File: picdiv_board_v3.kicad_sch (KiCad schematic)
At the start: 64 parts, among them J1 DC-Input, J10 PPS_B, J101 MountingHole_M2.5, J104 MountingHole_M2.5, J105 Conn_01x06, J106 PPS_A, J107 PPS_A, J14 TEST_1PPS, J4 SYNC, J6 PPS_B, J8 SYNC, SW101 SW_DIP_x03, U1 LT1963AxST-3.3, U103 LT1963AEQ, U104 LTC6993xS6-1, U105 IDT5PB1108, U2 LT1963AxST-3.3, U3 PIC12F675, U6 IDT5PB1108

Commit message: Remove redundant items.
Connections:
- net +6V renamed +5V
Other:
- note added: "5VDC for OXCO"
- note removed: "6VDC for sine-to-square"
- title: PICDIV - PPS-board - v3 -> PICDIV - PPS-board - v4 AF
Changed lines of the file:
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@@
 	(paper "A4")
 	(title_block
-		(title "PICDIV - PPS-board - v3")
-		(rev "2019-01")
+		(title "PICDIV - PPS-board - v4 AF")
+		(date "2024-11-19")
+		(rev "2024-11")
 		(company "anders.e.e.wallin \"at\" gmail.com")
 		(comment 1 "2018-08-01 first proto-boards order")
@@
 	)
 	(junction
+		(at 162.56 163.83)
+		(diameter 0)
+		(color 0 0 0 0)
+	)
+	(junction
 		(at 232.41 50.8)
 		(diameter 0)
@@
 	)
 	(junction
-		(at 161.29 163.83)
-		(diameter 0)
-		(color 0 0 0 0)
-	)
-	(junction
 		(at 140.97 140.97)
 		(diameter 0)
@@
 	(wire
 		(pts
-			(xy 161.29 163.83) (xy 161.29 161.29)
+			(xy 162.56 163.83) (xy 162.56 162.56)
 		)
 		(stroke
@@
 	(wire
 		(pts
+			(xy 162.56 163.83) (xy 163.83 163.83)
+		)
+		(stroke
+			(width 0)
+			(type default)
+		)
+	)
+	(wire
+		(pts
 			(xy 68.58 137.16) (xy 69.85 137.16)
 		)
@@
 	(wire
 		(pts
-			(xy 161.29 163.83) (xy 163.83 163.83)
-		)
-		(stroke
-			(width 0)
-			(type default)
-		)
-	)
-	(wire
-		(pts
 			(xy 115.57 53.34) (xy 121.92 53.34)
 		)
@@
 	(wire
 		(pts
-			(xy 151.13 163.83) (xy 161.29 163.83)
+			(xy 151.13 163.83) (xy 162.56 163.83)
 		)
 		(stroke
@@
 		)
 	)
-	(text "6VDC for sine-to-square"
+	(text "5VDC for OXCO"
 		(exclude_from_sim no)
 		(at 134.62 162.56 0)
@@
 	)
 	(symbol
-		(lib_id "power:+6V")
-		(at 161.29 161.29 0)
-		(unit 1)
-		(exclude_from_sim no)
-		(in_bom yes)
-		(on_board yes)
-		(dnp no)
-		(property "Reference" "#PWR017"
-			(at 161.29 165.1 0)
-			(effects
-				(font
-					(size 1.27 1.27)
-				)
-				(hide yes)
-			)
-		)
-		(property "Value" "+6V"
-			(at 161.29 157.734 0)
-			(effects
-				(font
-					(size 1.27 1.27)
-				)
-			)
-		)
-		(property "Footprint" ""
-			(at 161.29 161.29 0)
-			(effects
-				(font
-					(size 1.27 1.27)
-				)
-				(hide yes)
-			)
-		)
-		(property "Datasheet" ""
-			(at 161.29 161.29 0)
-			(effects
-				(font
-					(size 1.27 1.27)
-				)
-				(hide yes)
-			)
-		)
-		(property "Description" ""
-			(at 161.29 161.29 0)
-			(effects
-				(font
-					(size 1.27 1.27)
-				)
-				(hide yes)
-			)
-		)
-		(pin "1"
-		)
-		(instances
-			(project "picdiv_board_v3"
-				(path "/eba36321-b5f3-4bd6-a805-57b9b2ee447e"
-					(reference "#PWR017")
-					(unit 1)
-				)
-			)
-		)
-	)
-	(symbol
 		(lib_id "Device:D")
 		(at 31.75 163.83 180)
@@
 					(unit 1)
 				)
+			)
+		)
+	)
+	(symbol
+		(lib_id "power:+5V")
+		(at 162.56 162.56 0)
+		(unit 1)
+		(exclude_from_sim no)
+		(in_bom yes)
+		(on_board yes)
+		(dnp no)
+		(fields_autoplaced yes)
+		(property "Reference" "#PWR01"
+			(at 162.56 166.37 0)
+			(effects
+				(font
+					(size 1.27 1.27)
+				)
+				(hide yes)
+			)
+		)
+		(property "Value" "+5V"
+			(at 162.56 157.48 0)
+			(effects
+				(font
+					(size 1.27 1.27)
+				)
+			)
+		)
+		(property "Footprint" ""
+			(at 162.56 162.56 0)
+			(effects
+				(font
+					(size 1.27 1.27)
+				)
+				(hide yes)
+			)
+		)
+		(property "Datasheet" ""
+			(at 162.56 162.56 0)
+			(effects
+				(font
+					(size 1.27 1.27)
+				)
+				(hide yes)
+			)
+		)
+		(property "Description" "Power symbol creates a global label with name \"+5V\""
+			(at 162.56 162.56 0)
+			(effects
+				(font
+					(size 1.27 1.27)
+				)
+				(hide yes)
+			)
+		)
+		(pin "1"
+		)
+		(instances
+			(project ""
+				(path "/eba36321-b5f3-4bd6-a805-57b9b2ee447e"
+					(reference "#PWR01")
+					(unit 1)
+				)

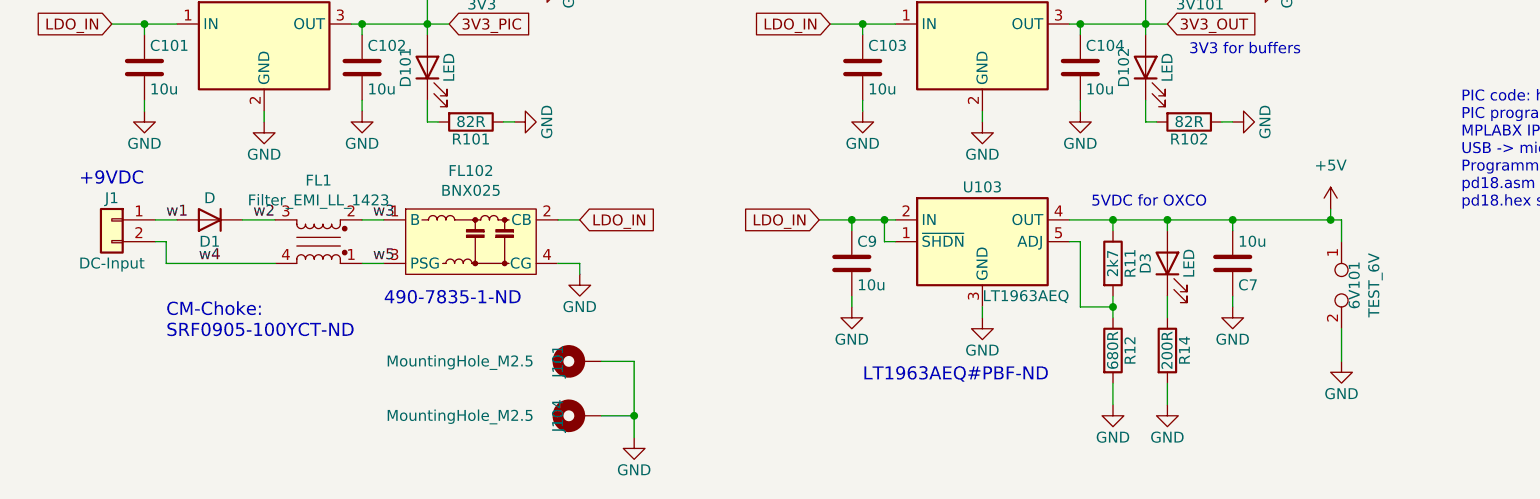
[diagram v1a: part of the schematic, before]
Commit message: 5.0V LDO for OXCO.
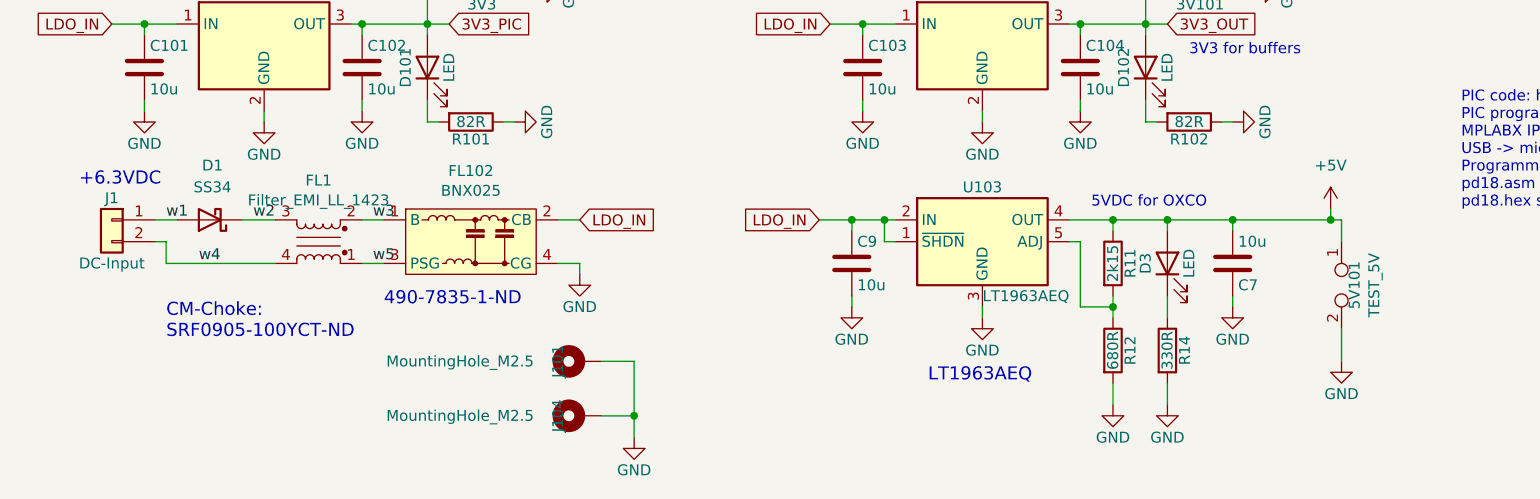
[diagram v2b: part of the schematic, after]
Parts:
- removed D1: D, awallinKiCadFootprints:DIODE_DO-214BA, symbol Device:D
- added D1: SS34, Diode_SMD:D_SMA, symbol Diode:SS34
- 5V101: renamed from 6V101; value TEST_6V -> TEST_5V
- R11: value 2k7 -> 2k15
- R14: value 200R -> 330R
- U103: LCSC (none) -> C459702
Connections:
- net w1: now also D1.2 (A)
- net w2: now also D1.1 (K)
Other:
- note added: "+6.3VDC"
- note added: "LT1963AEQ"
- note removed: "+9VDC"
- note removed: "LT1963AEQ#PBF-ND"
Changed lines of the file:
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@@
 		)
 	)
-	(text "LT1963AEQ#PBF-ND"
+	(text "LT1963AEQ"
 		(exclude_from_sim no)
-		(at 107.95 182.88 0)
+		(at 115.57 182.88 0)
 		(effects
 			(font
@@
 		)
 	)
-	(text "+9VDC"
+	(text "+6.3VDC"
 		(exclude_from_sim no)
 		(at 16.51 160.02 0)
@@
 			)
 		)
-		(property "Value" "2k7"
+		(property "Value" "2k15"
 			(at 137.16 168.91 90)
 			(effects
@@
 			)
 		)
-		(property "Value" "200R"
+		(property "Value" "330R"
 			(at 143.51 179.07 90)
 			(effects
@@
 	)
 	(symbol
-		(lib_id "Device:D")
-		(at 31.75 163.83 180)
-		(unit 1)
-		(exclude_from_sim no)
-		(in_bom yes)
-		(on_board yes)
-		(dnp no)
-		(property "Reference" "D1"
-			(at 31.75 166.37 0)
-			(effects
-				(font
-					(size 1.27 1.27)
-				)
-			)
-		)
-		(property "Value" "D"
-			(at 31.75 161.29 0)
-			(effects
-				(font
-					(size 1.27 1.27)
-				)
-			)
-		)
-		(property "Footprint" "awallinKiCadFootprints:DIODE_DO-214BA"
-			(at 31.75 163.83 0)
-			(effects
-				(font
-					(size 1.27 1.27)
-				)
-				(hide yes)
-			)
-		)
-		(property "Datasheet" ""
-			(at 31.75 163.83 0)
-			(effects
-				(font
-					(size 1.27 1.27)
-				)
-				(hide yes)
-			)
-		)
-		(property "Description" ""
-			(at 31.75 163.83 0)
-			(effects
-				(font
-					(size 1.27 1.27)
-				)
-				(hide yes)
-			)
-		)
-		(pin "1"
-		)
-		(pin "2"
-		)
-		(instances
-			(project "picdiv_board_v3"
-				(path "/eba36321-b5f3-4bd6-a805-57b9b2ee447e"
-					(reference "D1")
-					(unit 1)
-				)
-			)
-		)
-	)
-	(symbol
 		(lib_id "Device:R")
 		(at 134.62 41.91 0)
@@
 		(on_board yes)
 		(dnp no)
-		(property "Reference" "6V101"
+		(property "Reference" "5V101"
 			(at 165.354 171.45 0)
 			(effects
@@
 			)
 		)
-		(property "Value" "TEST_6V"
+		(property "Value" "TEST_5V"
 			(at 167.64 171.45 0)
 			(effects
@@
 			(project "picdiv_board_v3"
 				(path "/eba36321-b5f3-4bd6-a805-57b9b2ee447e"
-					(reference "6V101")
+					(reference "5V101")
 					(unit 1)
 				)
@@
 			)
 		)
+		(property "LCSC" "C459702 "
+			(at 121.92 166.37 0)
+			(effects
+				(font
+					(size 1.27 1.27)
+				)
+				(hide yes)
+			)
+		)
 		(pin "1"
 		)
@@
 					(unit 1)
 				)
+			)
+		)
+	)
+	(symbol
+		(lib_id "Diode:SS34")
+		(at 31.75 163.83 180)
+		(unit 1)
+		(exclude_from_sim no)
+		(in_bom yes)
+		(on_board yes)
+		(dnp no)
+		(fields_autoplaced yes)
+		(property "Reference" "D1"
+			(at 32.0675 157.48 0)
+			(effects
+				(font
+					(size 1.27 1.27)
+				)
+			)
+		)
+		(property "Value" "SS34"
+			(at 32.0675 160.02 0)
+			(effects
+				(font
+					(size 1.27 1.27)
+				)
+			)
+		)
+		(property "Footprint" "Diode_SMD:D_SMA"
+			(at 31.75 159.385 0)
+			(effects
+				(font
+					(size 1.27 1.27)
+				)
+				(hide yes)
+			)
+		)
+		(property "Datasheet" "https://www.vishay.com/docs/88751/ss32.pdf"
+			(at 31.75 163.83 0)
+			(effects
+				(font
+					(size 1.27 1.27)
+				)
+				(hide yes)
+			)
+		)
+		(property "Description" "40V 3A Schottky Diode, SMA"
+			(at 31.75 163.83 0)
+			(effects
+				(font
+					(size 1.27 1.27)
+				)
+				(hide yes)
+			)
+		)
+		(property "LCSC" "C8678"
+			(at 31.75 163.83 0)
+			(effects
+				(font
+					(size 1.27 1.27)
+				)
+				(hide yes)
+			)
+		)
+		(pin "2"
+		)
+		(pin "1"
+		)
+		(instances
+			(project ""
+				(path "/eba36321-b5f3-4bd6-a805-57b9b2ee447e"
+					(reference "D1")
+					(unit 1)
+				)

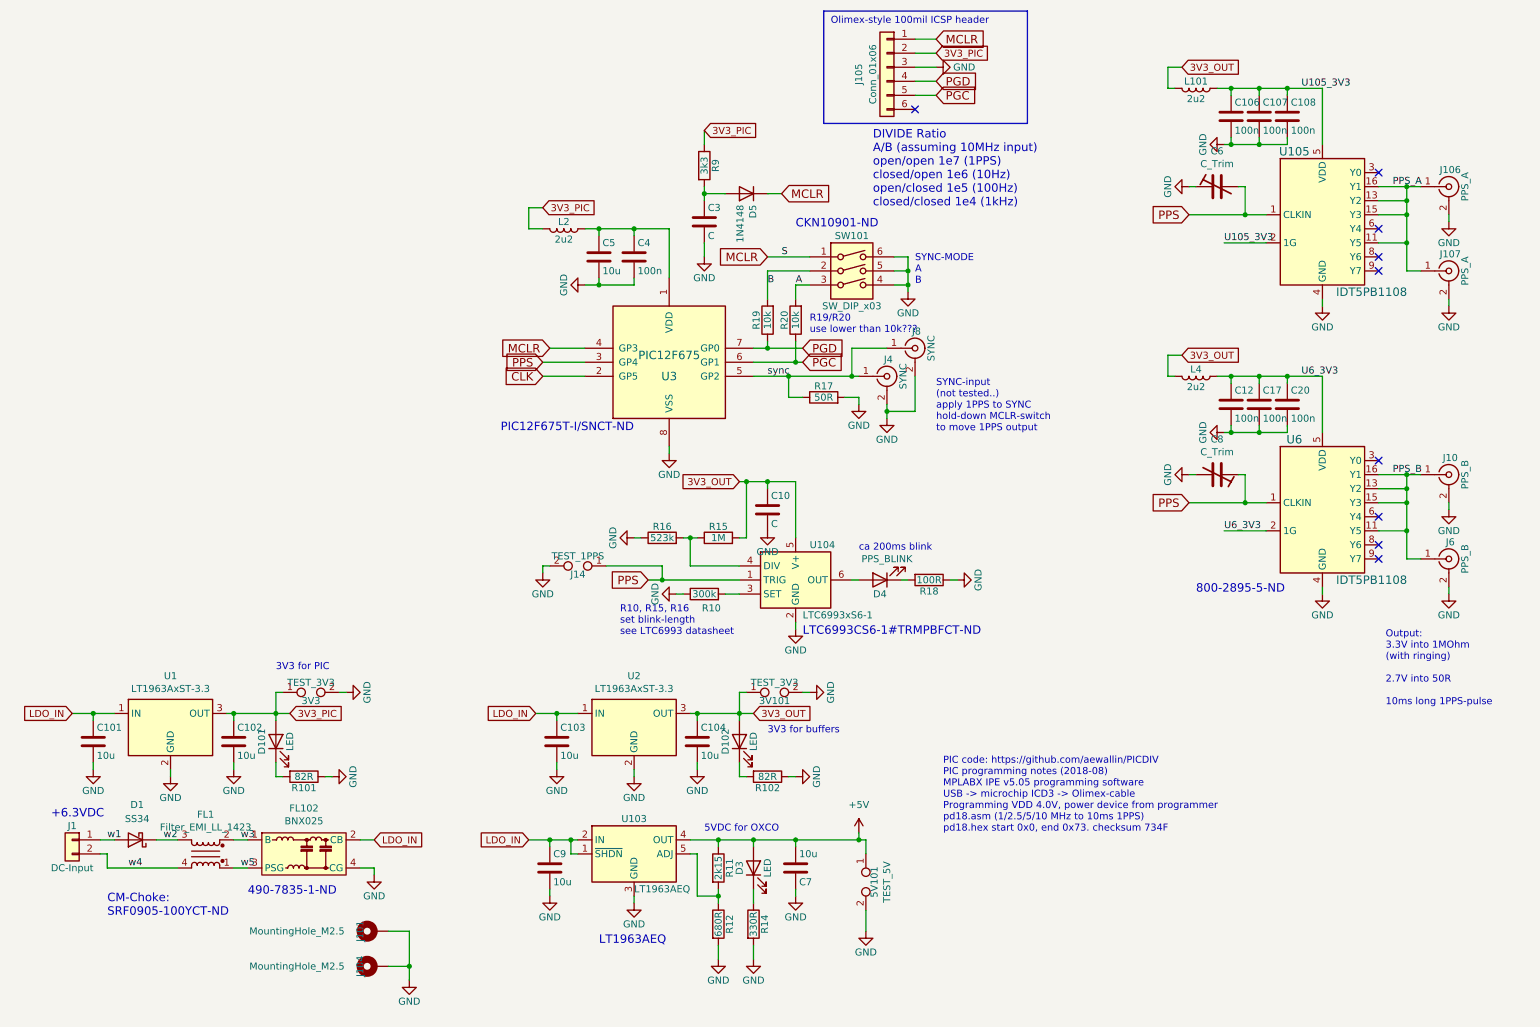
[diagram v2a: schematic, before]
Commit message: Add sheet for OXCO circuit
Putting the OXCO portion on a second sheet makes the schematic more better.
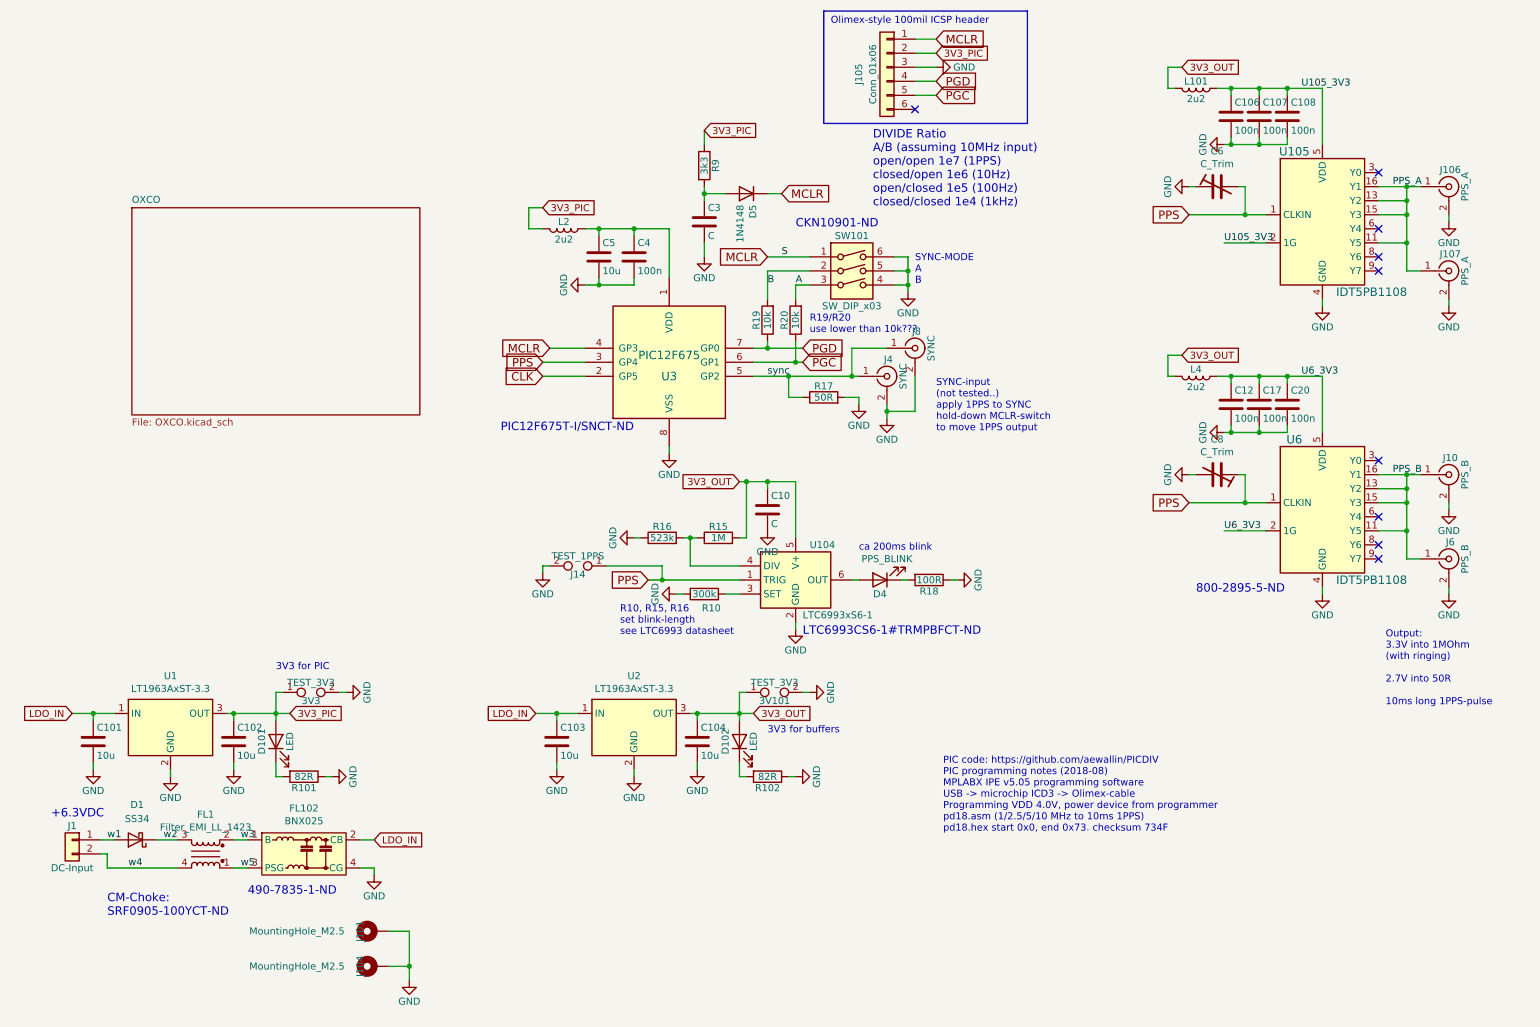
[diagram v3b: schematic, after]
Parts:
- removed 5V101: TEST_5V, TestPoint:TestPoint_2Pads_Pitch2.54mm_Drill0.8mm, symbol Connector:TestPoint_2Pole
- removed C7, C9: 10u, Capacitor_SMD:C_0805_2012Metric, symbol Device:C
- removed D3: LED, LED_SMD:LED_0805_2012Metric, symbol Device:LED
- removed R11: 2k15, Resistor_SMD:R_0805_2012Metric, symbol Device:R
- removed R12: 680R, Resistor_SMD:R_0805_2012Metric, symbol Device:R
- removed R14: 330R, Resistor_SMD:R_0805_2012Metric, symbol Device:R
- removed U103: LT1963AEQ, Package_TO_SOT_SMD:TO-263-5_TabPin3, symbol Regulator_Linear:LT1963AEQ
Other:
- added sheet OXCO (OXCO.kicad_sch)
- note removed: "5VDC for OXCO"
- note removed: "LT1963AEQ"

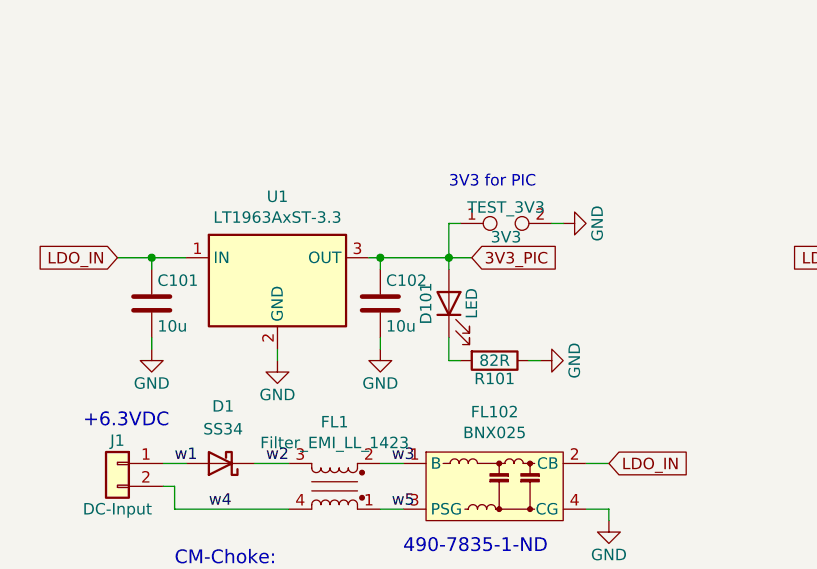
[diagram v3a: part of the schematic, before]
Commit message: More Vadj bits
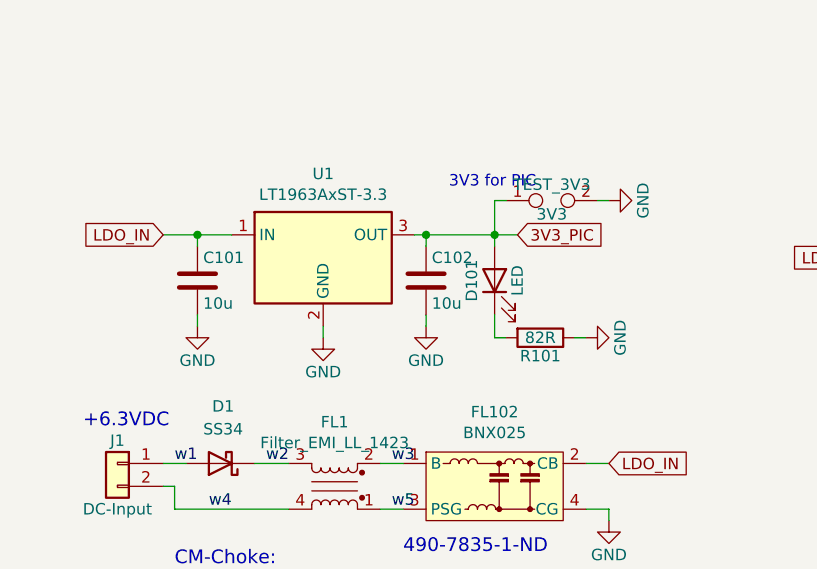
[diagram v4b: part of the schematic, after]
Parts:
- FL102: LCSC (none) -> C127891; MPN (none) -> BNX025H01L
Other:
- moved on the sheet: 3V3, C101, C102, D101, R101, U1

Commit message: OCXO Rev. 0
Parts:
- FL102: footprint Filter:Filter_Murata_BNX025_ThermalVias -> Filter:Filter_Murata_BNX025
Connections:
- net A: now also SW101.2; no longer SW101.3
- net B: now also SW101.1; no longer SW101.2
- net GND: no longer SW101.4
- net MCLR: no longer SW101.1
- net CLK renamed 10MHz
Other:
- moved on the sheet: SW101
